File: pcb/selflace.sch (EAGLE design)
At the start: 17 parts, among them J3 AVR_SPI_PROG_3X2NS, U1 ATMEGA328P_TQFP

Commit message: sending sch off for review
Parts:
- added C6: 0.33µF, SparkFun-Capacitors:0.33UF/330NF-0805-50V-10%
- added C7: 0.1uF, SparkFun-Capacitors:0.1UF-0603-25V-(+80/-20%)
- added C8, C9: 22pF, SparkFun-Capacitors:22PF-0603-50V-5%
- added IC1: 7805T, adafruit:7805T
- added J5: (no value), SparkFun-Connectors:CONN_02
- added J6: (no value), SparkFun-Connectors:CONN_02JST-PTH-2
- added J7: (no value), SparkFun-Connectors:CONN_03
- added R6, R7: 10k, SparkFun-Resistors:10KOHM-0603-1/10W-1%
- added S1: MOMENTARY-SWITCH-SPST-PTH-6.0MM, SparkFun-Switches:MOMENTARY-SWITCH-SPST-PTH-6.0MM
- added VR1: 10k, SparkFun-Resistors:POTENTIOMETER-PTH-9MM-1/20W-20%
- added Y1: 16MHz, SparkFun-Clocks:CRYSTAL-16MHZPTH-HC49US
- R5: value 1k -> 10k; device SparkFun-Resistors:1KOHM-0603-1/10W-1% -> SparkFun-Resistors:10KOHM-0603-1/10W-1%
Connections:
- new net DIG5: U1.PD5(T1), U2.IN2
- new net DIG6: U1.PD6(AIN0), U2.IN1
- new net N$1: R6.2, S1.1, U1.PD4(XCK/T0)
- new net N$11: C9.1, U1.PB7(XTAL2/TOSC2), Y1.1
- new net N$12: C6.1, IC1.VI, J6.1, J7.3
- new net N$2: J5.2, R7.2, U1.PD7(AIN1)
- net GND: now also C6.2, C7.2, C8.2, C9.2, IC1.GND, J6.2, J7.2, R6.1, R7.1, VR1.A
- net N$6: now also U1.PC2(ADC2), VR1.S; no longer U1.PB1(OC1A), U2.IN1
- net N$7: now also C8.1, U1.PB6(XTAL1/TOSC1), Y1.2; no longer U1.PB2(SS/OC1B), U2.IN2
- net VCC: now also C7.1, IC1.VO, J5.1, S1.2, U1.AREF, VR1.E
- net VCC_1: now also J7.1
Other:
- moved on the sheet: C1, C2, C3, C5, J1, J2, R1, R2, R3, R4, U2

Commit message: maybe finish schematic, sending off for review
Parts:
- added C10, C12: 1.0uF, SparkFun-Capacitors:1.0UF-0603-16V-10%
- added C11, C13: 0.1uF, SparkFun-Capacitors:0.1UF-0603-25V-(+80/-20%)
- added C14: 100uF, SparkFun-Capacitors:100UF-POLAR-10X10.5-63V-20%
- C6: value 0.33µF -> 1.0uF; device SparkFun-Capacitors:0.33UF/330NF-0805-50V-10% -> SparkFun-Capacitors:1.0UF-0603-16V-10%
- IC1: value 7805T -> 78L05Z; device adafruit:7805T -> linear:78L05Z
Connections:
- net GND: now also C10.2, C11.2, C12.2, C13.2, C14.-, C6.1, J6.1; no longer C6.2, J6.2
- net N$12: now also C14.+, C6.2, J6.2; no longer C6.1, J6.1
- net N$3: now also R3.1; no longer R3.2
- net VCC: now also C10.1, C11.1, C12.1, C13.1, R3.2; no longer R3.1
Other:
- note added: "Microcontroller/Support"
- note added: "Motor Controller"
- note added: "Power"
- note added: "Programming Headers"
- moved on the sheet: C1, C2, C3, C4, C5, C6, C7, C8, C9, IC1, J1, J2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

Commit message: nearly done! sending off for final review
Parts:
- added C15: 0.1uF, SparkFun-Capacitors:0.1UF-0603-25V-(+80/-20%)
- added D1: FWD, SparkFun-LED:LED-BLUE1206
- added D2: BKWD, SparkFun-LED:LED-RED1206
- added D3: POWER, SparkFun-LED:LED-GREEN1206
- added D4: STATE, SparkFun-LED:LED-GREEN1206
- added LOGO1: OSHW-LOGOM, SparkFun-Aesthetics:OSHW-LOGOM
- added MGT1, MGT2, MGT3, MGT4: BEAGLEBONEBLACK_MOUNTING_HOLE, BeagleBone_Black_Wireless:BEAGLEBONEBLACK_MOUNTING_HOLE
- added R10, R11, R8, R9: 220, SparkFun-Resistors:220OHM-0603-1/10W-1%
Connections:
- new net DIG2: R8.1, U1.PD2(INT0)
- new net DIG3: R9.1, U1.PD3(INT1)
- new net DIG8: R10.1, U1.PB0(ICP)
- new net DIG9: R11.1, U1.PB1(OC1A)
- new net N$13: D1.A, R8.2
- new net N$14: D2.A, R9.2
- new net N$15: D3.A, R10.2
- new net N$16: D4.A, R11.2
- net GND: now also C15.2, D1.C, D2.C, D3.C, D4.C, MGT1.P$1, MGT2.P$1, MGT3.P$1, MGT4.P$1
- net VCC: now also C15.1
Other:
- note added: "Indicators/Misc"

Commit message: update board to size specs and increase power/ground trace width
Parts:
- removed D1: FWD, SparkFun-LED:LED-BLUE1206
- removed D2: BKWD, SparkFun-LED:LED-RED1206
- removed D3: POWER, SparkFun-LED:LED-GREEN1206
- removed D4: STATE, SparkFun-LED:LED-GREEN1206
- removed FRAME1: FRAME-LEDGER, SparkFun-Aesthetics:FRAME-LEDGER
- removed R10, R11, R8, R9: 220, SparkFun-Resistors:220OHM-0603-1/10W-1%
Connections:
- removed net N$13: D1.A, R8.2
- removed net N$14: D2.A, R9.2
- removed net N$15: D3.A, R10.2
- removed net N$16: D4.A, R11.2
- net DIG2: no longer R8.1
- net DIG3: no longer R9.1
- net DIG8: no longer R10.1
- net DIG9: no longer R11.1
- net GND: no longer D1.C, D2.C, D3.C, D4.C

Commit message: add sch border back, fix wire stubs
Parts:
- added FRAME1: FRAME-LEDGER, SparkFun-Aesthetics:FRAME-LEDGER
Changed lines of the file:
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@@
 <part name="C15" library="SparkFun-Capacitors" library_urn="urn:adsk.eagle:library:510" deviceset="0.1UF" device="-0603-25V-(+80/-20%)" package3d_urn="urn:adsk.eagle:package:37414/1" value="0.1uF"/>
 <part name="SUPPLY10" library="SparkFun-PowerSymbols" library_urn="urn:adsk.eagle:library:530" deviceset="VCC" device=""/>
+<part name="FRAME1" library="SparkFun-Aesthetics" library_urn="urn:adsk.eagle:library:507" deviceset="FRAME-LEDGER" device="" package3d_urn="urn:adsk.eagle:package:37121/1"/>
 </parts>
 <sheets>
@@
 <attribute name="VALUE" x="-15.24" y="18.034" size="1.778" layer="96" align="bottom-center"/>
 </instance>
+<instance part="FRAME1" gate="G$1" x="-132.08" y="-88.9" smashed="yes"/>
+<instance part="FRAME1" gate="G$2" x="198.12" y="-88.9" smashed="yes">
+<attribute name="LAST_DATE_TIME" x="210.82" y="-87.63" size="2.54" layer="94" font="vector"/>
+<attribute name="SHEET" x="284.48" y="-87.63" size="2.54" layer="94" font="vector"/>
+<attribute name="DRAWING_NAME" x="213.614" y="-71.12" size="2.7432" layer="94" font="vector"/>
+</instance>
 </instances>

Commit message: routing is hell and i hate it
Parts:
- removed C1, C11: 0.1uF, SparkFun-Capacitors:0.1UF-0603-25V-(+80/-20%)
- removed C10, C5: 1.0uF, SparkFun-Capacitors:1.0UF-0603-16V-10%
- added D1, D2, D3, D4: (no value), SparkFun-LED:LED1206
- added R10, R11, R8, R9: 220, SparkFun-Resistors:220OHM-0603-1/10W-1%
- Y1: device SparkFun-Clocks:CRYSTAL-16MHZPTH-HC49US -> SparkFun-Clocks:CRYSTAL-16MHZSMD-5X3.2
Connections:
- new net N$14: D1.A, R8.2
- new net N$15: D2.A, R9.2
- new net N$16: D3.A, R10.2
- new net N$17: D4.A, R11.2
- net DIG2: now also R8.1
- net DIG3: now also R9.1
- net DIG8: now also R10.1
- net DIG9: now also R11.1
- net GND: now also D1.C, D2.C, D3.C, D4.C; no longer C1.2, C10.2, C11.2, C5.2
- net VCC: no longer C1.1, C10.1, C11.1, C5.1

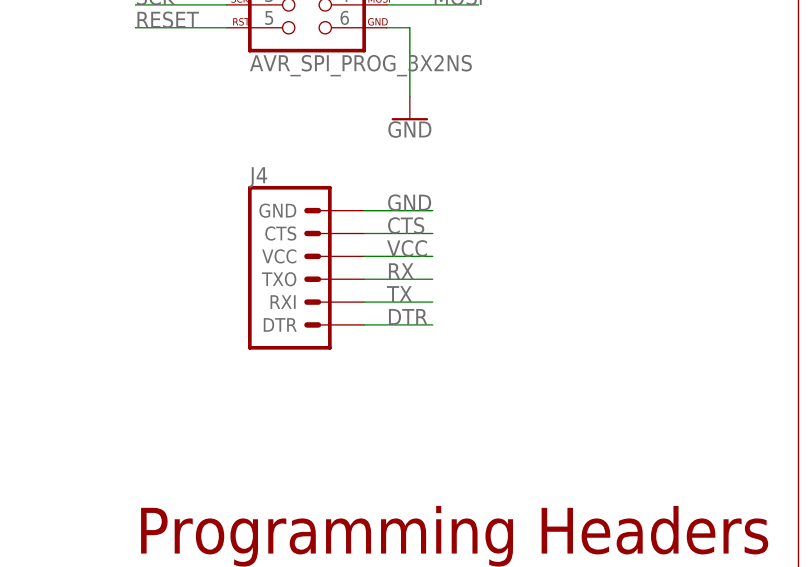
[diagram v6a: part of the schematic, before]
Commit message: fix rx/tx, not present on in-class pcb
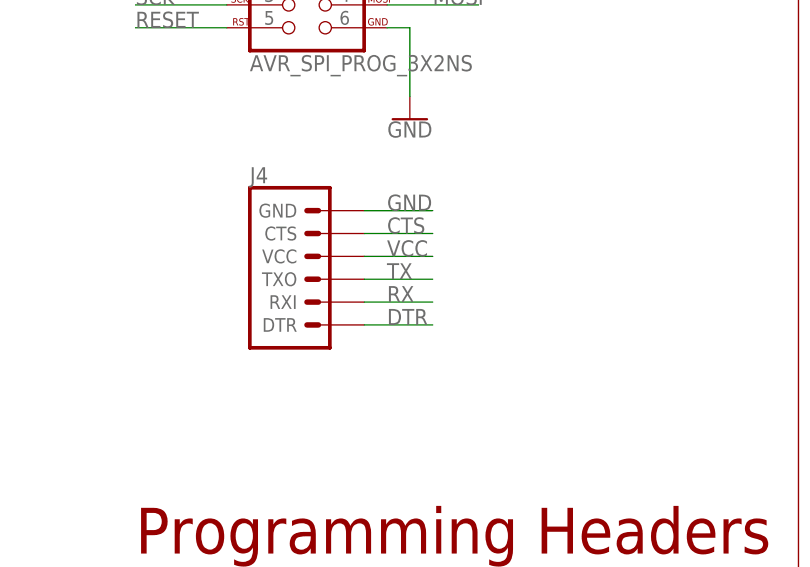
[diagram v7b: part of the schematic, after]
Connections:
- net RX: now also J4.RXI; no longer J4.TXO
- net TX: now also J4.TXO; no longer J4.RXI
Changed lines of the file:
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@@
 <net name="RX" class="0">
+<segment>
+<pinref part="U1" gate="U$1" pin="PD0(RXD)"/>
+<wire x1="50.8" y1="7.62" x2="60.96" y2="7.62" width="0.1524" layer="91"/>
+<label x="55.88" y="7.62" size="1.778" layer="95"/>
+</segment>
+<segment>
+<pinref part="J4" gate="G$1" pin="RXI"/>
+<wire x1="55.88" y1="127" x2="63.5" y2="127" width="0.1524" layer="91"/>
+<label x="58.42" y="127" size="1.778" layer="95"/>
+</segment>
+</net>
+<net name="TX" class="0">
+<segment>
+<pinref part="U1" gate="U$1" pin="PD1(TXD)"/>
+<wire x1="50.8" y1="5.08" x2="60.96" y2="5.08" width="0.1524" layer="91"/>
+<label x="55.88" y="5.08" size="1.778" layer="95"/>
+</segment>
 <segment>
 <pinref part="J4" gate="G$1" pin="TXO"/>
@@
 <label x="58.42" y="129.54" size="1.778" layer="95"/>
 </segment>
-<segment>
-<pinref part="U1" gate="U$1" pin="PD0(RXD)"/>
-<wire x1="50.8" y1="7.62" x2="60.96" y2="7.62" width="0.1524" layer="91"/>
-<label x="55.88" y="7.62" size="1.778" layer="95"/>
-</segment>
 </net>
-<net name="TX" class="0">
-<segment>
-<pinref part="J4" gate="G$1" pin="RXI"/>
-<wire x1="55.88" y1="127" x2="63.5" y2="127" width="0.1524" layer="91"/>
-<label x="58.42" y="127" size="1.778" layer="95"/>
-</segment>
-<segment>
-<pinref part="U1" gate="U$1" pin="PD1(TXD)"/>
-<wire x1="50.8" y1="5.08" x2="60.96" y2="5.08" width="0.1524" layer="91"/>
-<label x="55.88" y="5.08" size="1.778" layer="95"/>
-</segment>
-</net>
